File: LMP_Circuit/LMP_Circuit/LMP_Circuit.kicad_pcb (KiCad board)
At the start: 2 copper layers, 126.5 x 91.7 mm, 3 parts

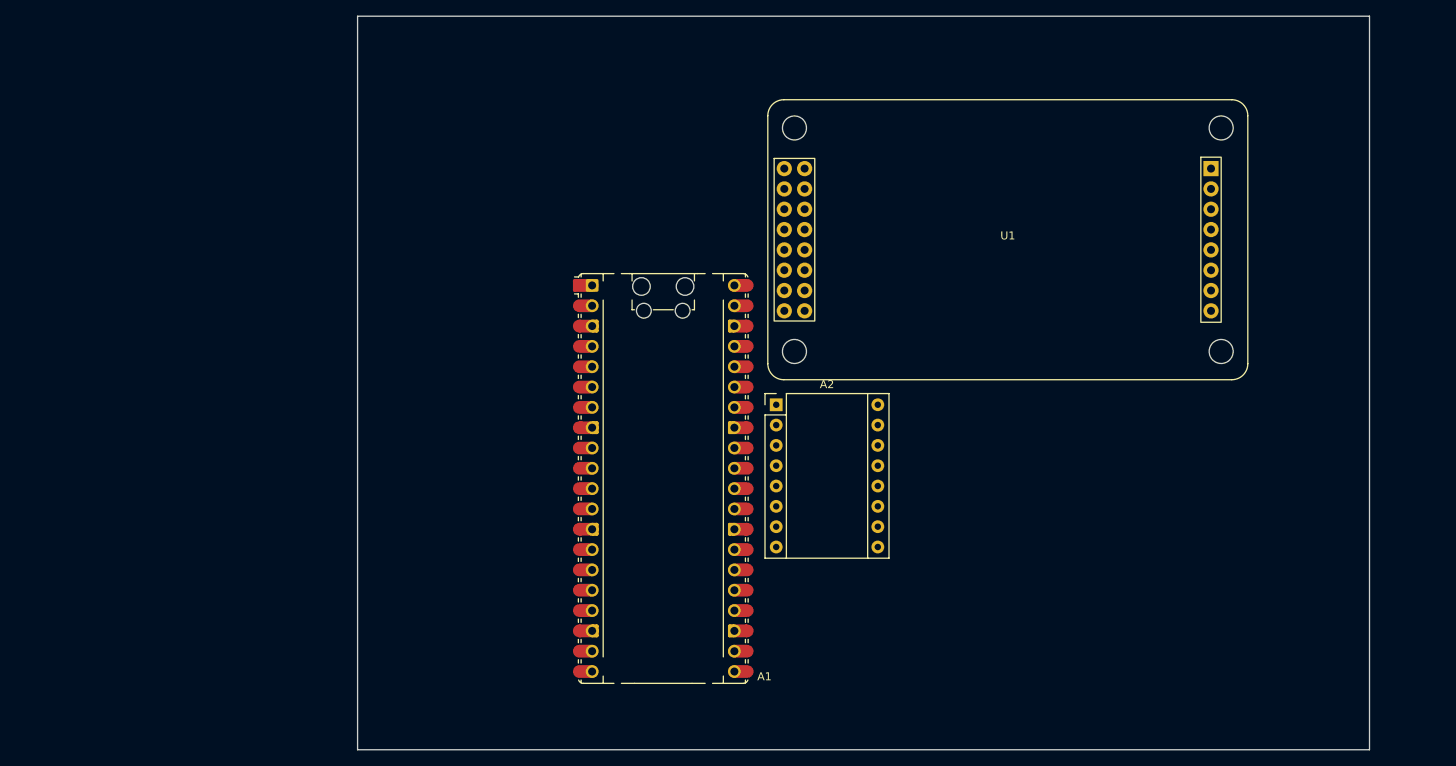
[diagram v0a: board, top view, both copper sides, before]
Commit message: added power converter diagram and relay.
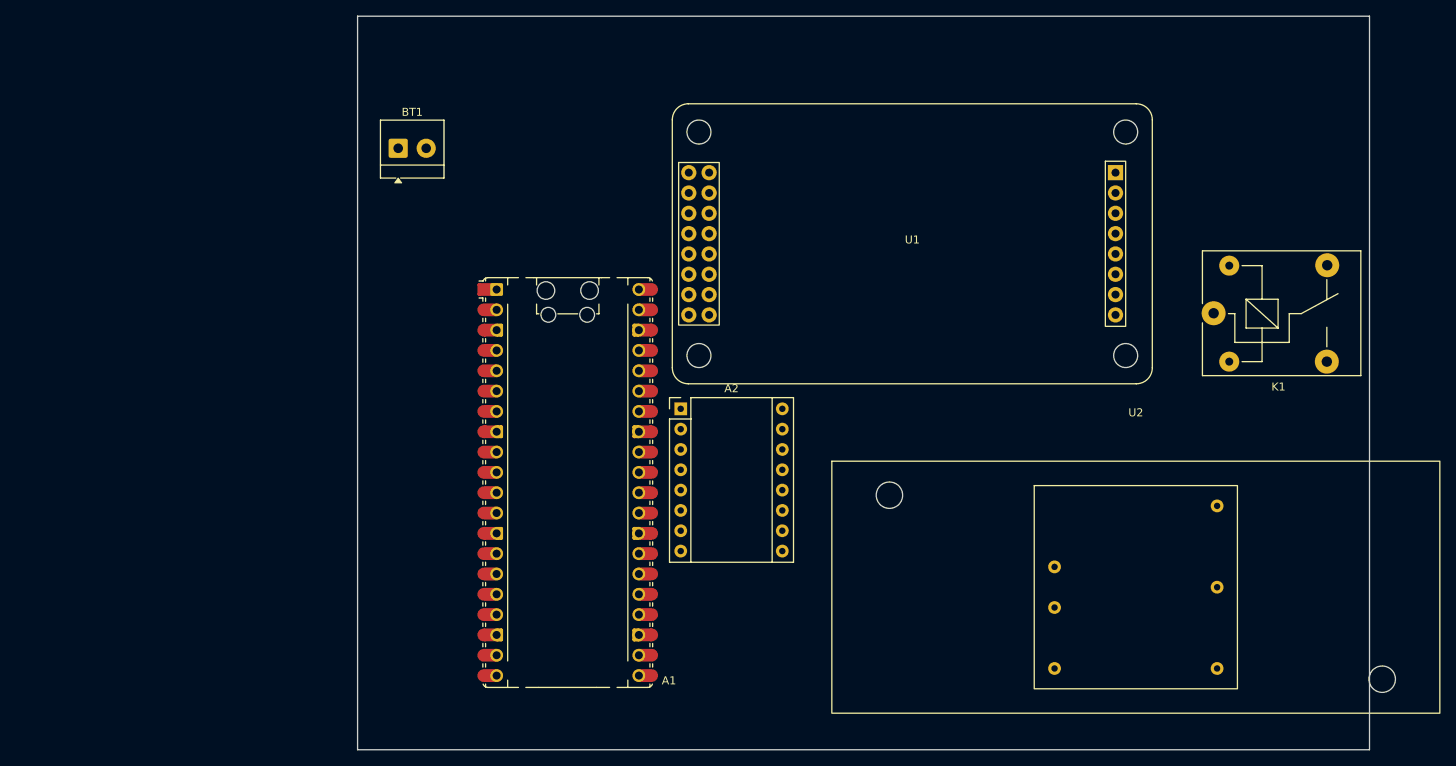
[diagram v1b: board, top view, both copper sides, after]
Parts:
- added BT1: Battery, TerminalBlock_4Ucon:TerminalBlock_4Ucon_1x02_P3.50mm_Horizontal, F.Cu at (104.9, 74.2)
- added K1: SANYOU_SRD_Form_C, Relay_THT:Relay_SPDT_SANYOU_SRD_Series_Form_C, F.Cu at (206.8, 94.8)
- added U2: DQD2_Single, External/Custom Parts:DQD20, F.Cu at (197.1, 129.0)
- moved A1 11.9 mm to (126.1, 116.0)
- moved U1 11.9 mm to (169.2, 86.1)
- moved A2 11.9 mm to (140.2, 106.7)
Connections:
- A1 pad 1: unconnected-(A1-GPIO0-Pad1) -> /Relay_Trigger

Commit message: initial layout created.
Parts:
- removed A2: Pololu_Breakout_A4988, Module:Pololu_Breakout-16_15.2x20.3mm
- removed BT1: Battery, TerminalBlock_4Ucon:TerminalBlock_4Ucon_1x02_P3.50mm_Horizontal
- removed K1: SANYOU_SRD_Form_C, Relay_THT:Relay_SPDT_SANYOU_SRD_Series_Form_C
- removed U2: DQD2_Single, External/Custom Parts:DQD20
- added A3: Pololu_Breakout_A4988, Module:Pololu_Breakout-16_15.2x20.3mm, F.Cu at (125.0, 102.9)
- added C1: 100nf, Capacitor_SMD:C_0603_1608Metric, B.Cu at (110.5, 77.7)
- added C2: 10uf, Capacitor_SMD:C_0603_1608Metric, B.Cu at (114.6, 81.8)
- added C3: 100n, Capacitor_SMD:C_0603_1608Metric, B.Cu at (117.9, 81.8)
- added C4: 10uf, Capacitor_SMD:C_0603_1608Metric, B.Cu at (122.7, 81.8)
- added C5: 100nf, Capacitor_SMD:C_0603_1608Metric, B.Cu at (126.0, 81.8)
- added C6: 10uf, Capacitor_SMD:C_0603_1608Metric, B.Cu at (116.6, 89.4)
- added J1: SCLK, Connector_PinHeader_1.00mm:PinHeader_1x02_P1.00mm_Vertical, B.Cu at (90.5, 112.5)
- added J10: RX, Connector_PinHeader_1.00mm:PinHeader_1x01_P1.00mm_Vertical, B.Cu at (100.1, 133.3)
- added J11: Stepper_Terminals, TerminalBlock_4Ucon:TerminalBlock_4Ucon_1x04_P3.50mm_Horizontal, B.Cu at (122.9, 118.5)
- added J12: ISO_Power_Terminal, TerminalBlock_4Ucon:TerminalBlock_4Ucon_1x02_P3.50mm_Horizontal, B.Cu at (102.9, 76.5)
- added J2: MOSI, Connector_PinHeader_1.00mm:PinHeader_1x02_P1.00mm_Vertical, B.Cu at (87.1, 112.5)
- added J3: MISO, Connector_PinHeader_1.00mm:PinHeader_1x02_P1.00mm_Vertical, B.Cu at (83.8, 112.5)
- added J4: MISO, Connector_PinHeader_1.00mm:PinHeader_1x02_P1.00mm_Vertical, B.Cu at (80.5, 112.5)
- added J5: Relay_Trig, Connector_PinHeader_1.00mm:PinHeader_1x01_P1.00mm_Vertical, B.Cu at (99.8, 122.9)
- added J6: Power Terminal, TerminalBlock_4Ucon:TerminalBlock_4Ucon_1x03_P3.50mm_Horizontal, B.Cu at (117.0, 76.2)
- added J7: Electrode+, Connector_Coaxial:BNC_TEConnectivity_1478035_Horizontal, F.Cu at (74.1, 72.8)
- added J8: Electrode-, Connector_Coaxial:BNC_TEConnectivity_1478035_Horizontal, F.Cu at (91.2, 73.5)
- added J9: TX, Connector_PinHeader_1.00mm:PinHeader_1x01_P1.00mm_Vertical, B.Cu at (100.6, 128.5)
- added R10: 1k, Resistor_SMD:R_0603_1608Metric_Pad0.98x0.95mm_HandSolder, B.Cu at (121.4, 90.9)
- added R11: 1k, Resistor_SMD:R_0603_1608Metric_Pad0.98x0.95mm_HandSolder, B.Cu at (112.8, 103.9)
- added R3: 5M, Resistor_SMD:R_0603_1608Metric_Pad0.98x0.95mm_HandSolder, B.Cu at (116.6, 86.4)
- added R5: 23.57k, Resistor_SMD:R_0603_1608Metric_Pad0.98x0.95mm_HandSolder, B.Cu at (58.4, 110.2)
- added R6: 3.84k, Resistor_SMD:R_0603_1608Metric_Pad0.98x0.95mm_HandSolder, B.Cu at (58.4, 113.8)
- added R7: 23.57k, Resistor_SMD:R_0603_1608Metric_Pad0.98x0.95mm_HandSolder, B.Cu at (58.4, 120.7)
- added R8: 3.84k, Resistor_SMD:R_0603_1608Metric_Pad0.98x0.95mm_HandSolder, B.Cu at (58.4, 124.1)
- added R9: 1M, Resistor_SMD:R_0603_1608Metric_Pad0.98x0.95mm_HandSolder, B.Cu at (121.4, 87.1)
- added U3: ISO124U/1K, External/Custom Parts:ISO124U, B.Cu at (94.9, 93.8)
- added U4: ADS1256, External/Custom Parts:ADS1256, F.Cu at (89.7, 122.9)
- U1: value ~ -> ISO124U/1K; footprint External/Custom Parts:ADS1256 -> External/Custom Parts:ISO124U; moved to B.Cu
- moved U1 93.4 mm to (76.1, 93.8), turned to 90 degrees
- moved A1 47.9 mm to (83.9, 93.2), turned to 90 degrees
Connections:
- A1 pad 1: /Relay_Trigger -> /TX
- A1 pad 2: unconnected-(A1-GPIO1-Pad2) -> /RX
- A1 pad 20: unconnected-(A1-GPIO15-Pad20) -> /PhotoMos
- A1 pad 27: unconnected-(A1-GPIO21-Pad27) -> Net-(A1-GPIO21)
- A1 pad 29: unconnected-(A1-GPIO22-Pad29) -> Net-(A1-GPIO22)
- A1 pad 36: unconnected-(A1-3V3-Pad36) -> +3.3V
- A1 pad 4: unconnected-(A1-GPIO2-Pad4) -> /Relay_Trigger
- U1 pad 1: +5V -> Probe_28V
- U1 pad 13: unconnected-(U1-A4-Pad13) -> Net-(U1-VOUT)
- U1 pad 14: unconnected-(U1-A5-Pad14) -> GND
- U1 pad 15: unconnected-(U1-A6-Pad15) -> 28V
- U1 pad 16: unconnected-(U1-A7-Pad16) -> GND
- U1 pad 2: GND -> GND1
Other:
- board size 126.5 x 91.7 mm -> 70 x 70 mm

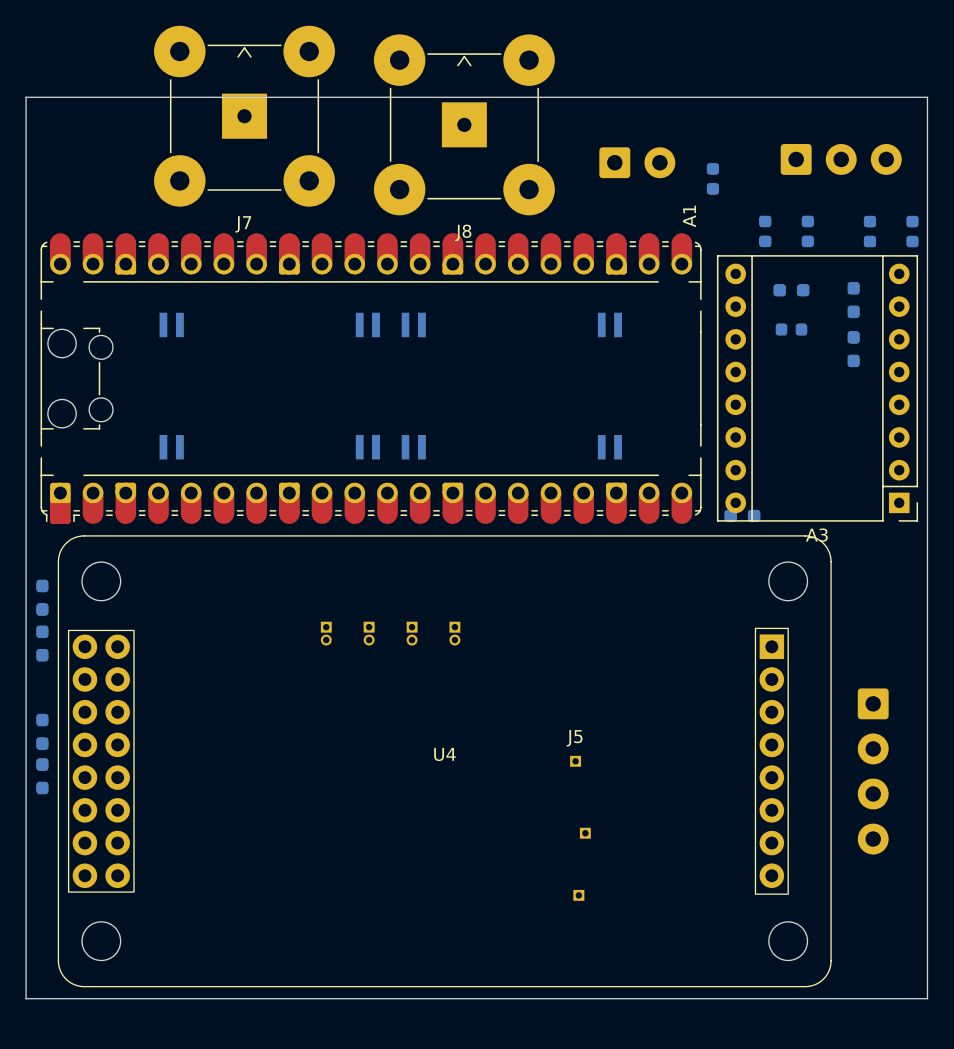
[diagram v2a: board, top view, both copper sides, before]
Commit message: Fully routed, lacks photomosfet
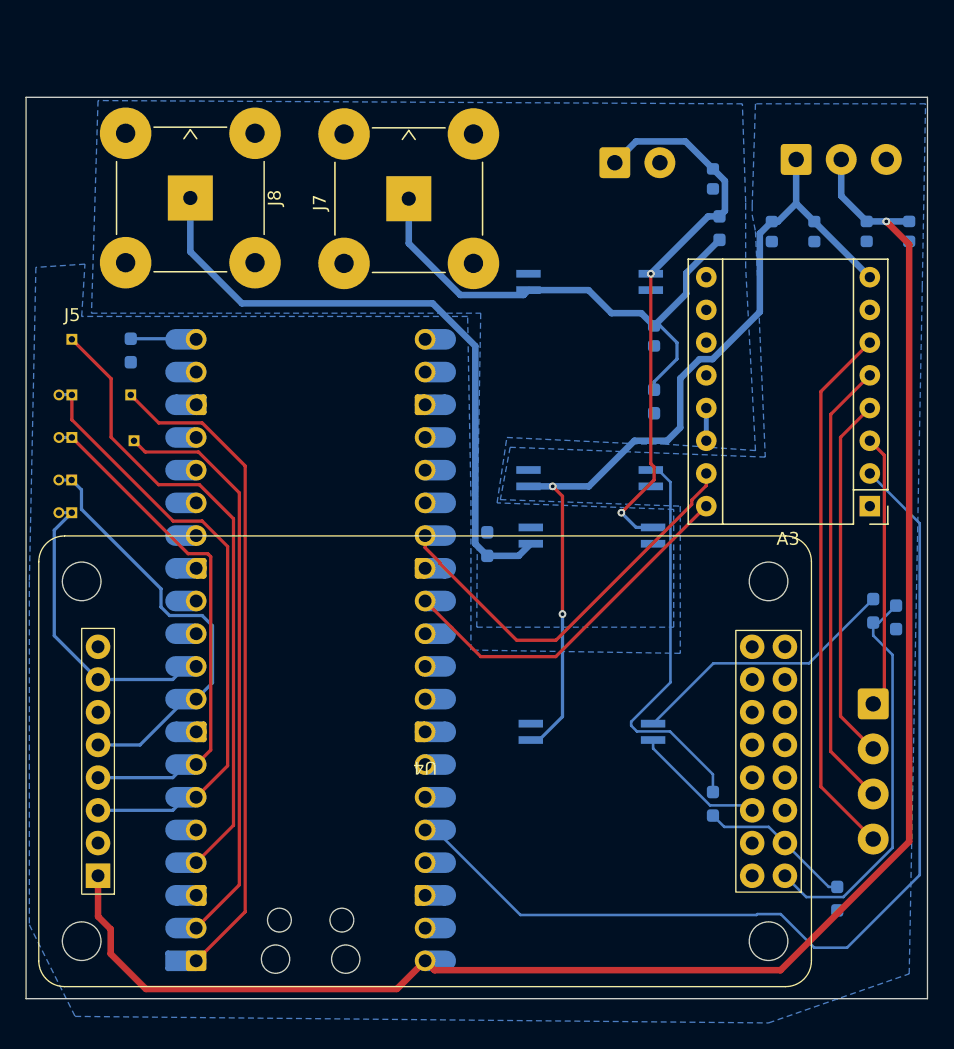
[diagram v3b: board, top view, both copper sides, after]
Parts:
- A1: moved to B.Cu
- moved R6 66.3 mm to (124.7, 111.8)
- moved R5 64.5 mm to (122.9, 111.3)
- moved R8 62.4 mm to (120.1, 133.6)
- moved R7 52.4 mm to (110.5, 126.2)
- moved J5 51.0 mm to (60.7, 90.2)
- moved J10 49.4 mm to (65.5, 98.0), turned to 90 degrees
- moved R11 49.2 mm to (65.3, 91.0), turned to 90 degrees
- moved J9 49.0 mm to (65.3, 94.5), turned to 90 degrees
- moved J1 34.8 mm to (60.7, 94.5), turned to 90 degrees
- moved U1 31.6 mm to (101.1, 113.0), turned to 180 degrees
- moved R3 30.8 mm to (93.0, 106.1), turned to 90 degrees
- moved J2 30.2 mm to (60.7, 97.8), turned to 90 degrees
- moved J3 25.8 mm to (60.7, 101.1), turned to 90 degrees
- moved J8 22.0 mm to (69.9, 79.2)
- moved J4 21.7 mm to (60.7, 103.6), turned to 90 degrees
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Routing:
- net +5V: track 0.00 -> 132.8 mm, vias 0 -> 1
- net +3.3V: track 0.00 -> 76.6 mm
- net 28V: track 0.00 -> 68.6 mm, vias 0 -> 2
- net /TX: track 0.00 -> 51.2 mm
- net /Electrode-: track 0.00 -> 49.8 mm
- net /Relay_Trigger: track 0.00 -> 48.9 mm
- net /SCLK: track 0.00 -> 46.8 mm
- net /RX: track 0.00 -> 45.0 mm
- net Probe_28V: track 0.00 -> 43.3 mm, vias 0 -> 2
- net /2B: track 0.00 -> 41.8 mm
- net /Bias_Sweep: track 0.00 -> 41.0 mm
- net /MOSI: track 0.00 -> 39.5 mm
- net /2A: track 0.00 -> 35.1 mm
- net /MISO: track 0.00 -> 32.9 mm
- net Net-(A1-GPIO21): track 0.00 -> 31.9 mm
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- added copper zone on B.Cu, net GND
- added copper zone on B.Cu, net GND1

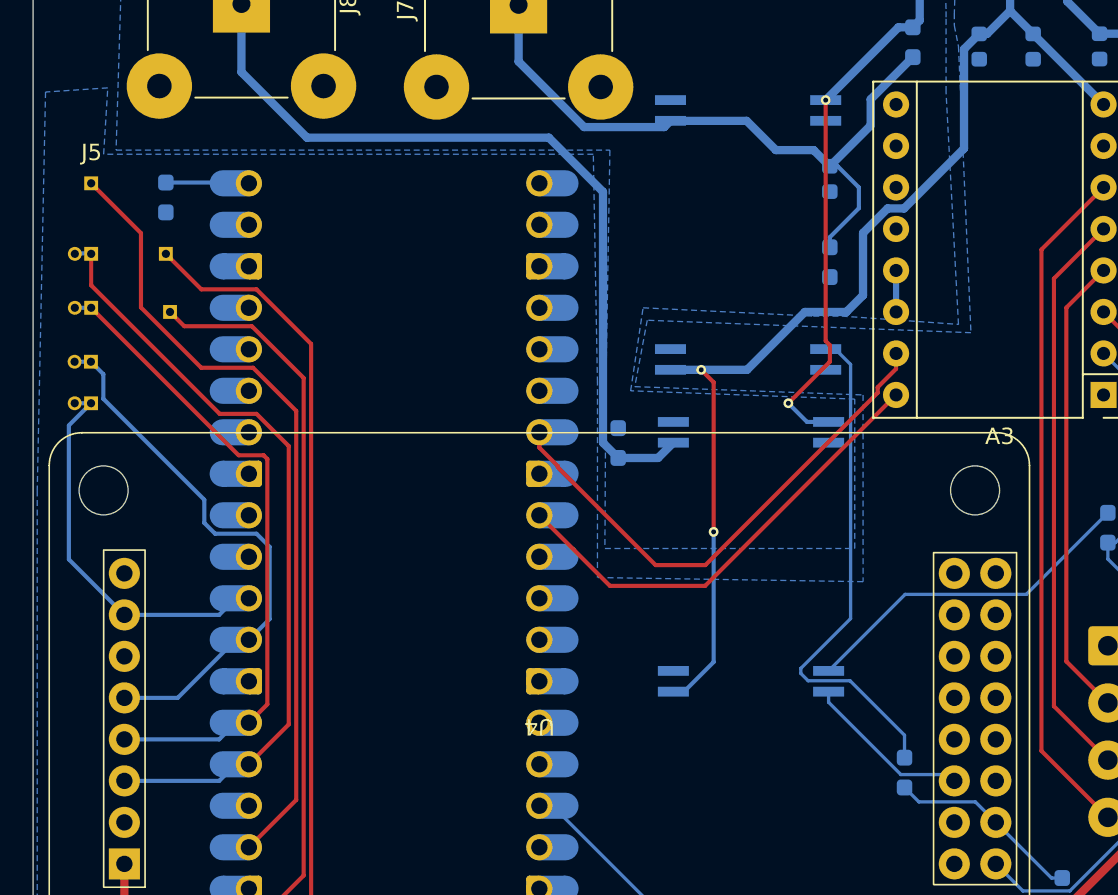
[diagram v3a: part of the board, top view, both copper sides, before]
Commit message: Added Photomos. finished layout
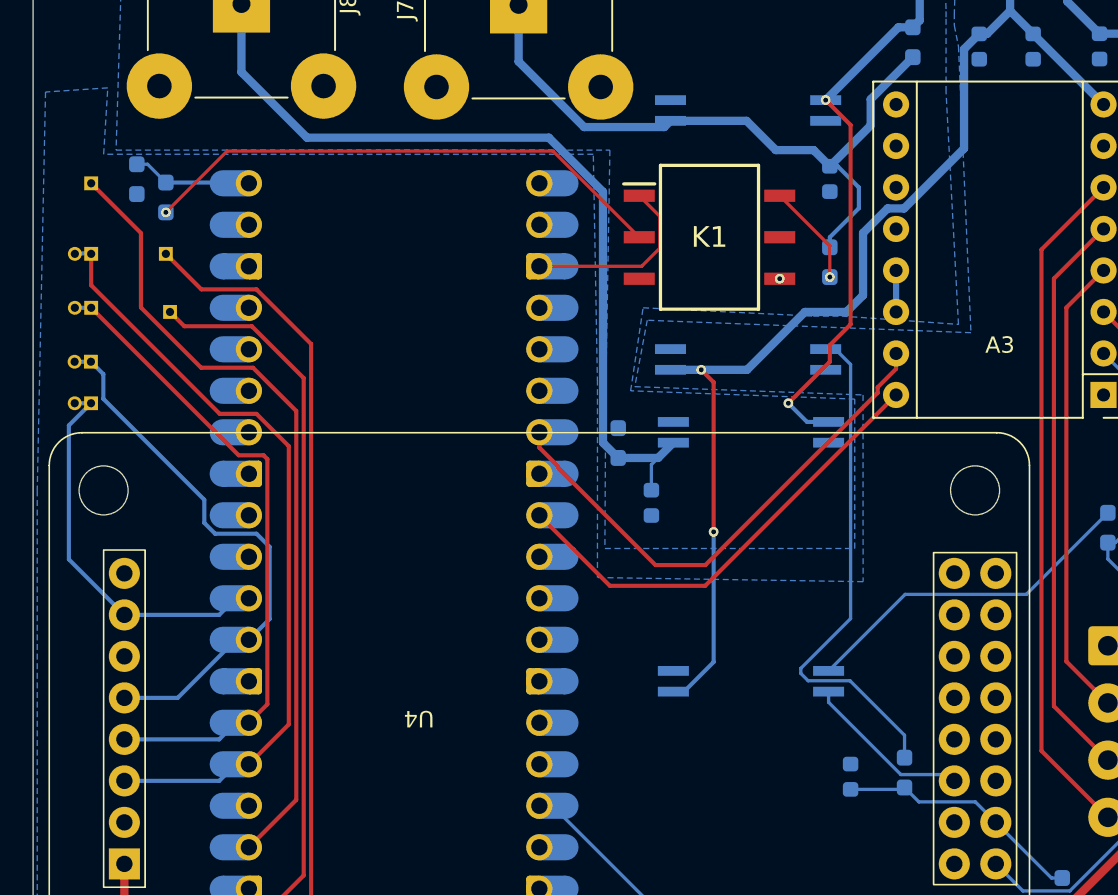
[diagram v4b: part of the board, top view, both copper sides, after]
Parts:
- added C7: 1uf, Capacitor_SMD:C_0603_1608Metric, B.Cu at (107.2, 126.5)
- added C8: 300nf, Capacitor_SMD:C_0603_1608Metric, B.Cu at (95.0, 109.7)
- added K1: AQV101AZ, AQV101AZ:SOP254P960X390-6N, F.Cu at (98.6, 93.5)
- added R1: 1k, Resistor_SMD:R_0603_1608Metric_Pad0.98x0.95mm_HandSolder, B.Cu at (63.5, 89.9)
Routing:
- net Net-(K1-K): track 0.00 -> 32.7 mm, vias 0 -> 1
- net GND: track 10.3 -> 21.9 mm
- net Net-(K1-OUT_2): track 0.00 -> 6.25 mm, vias 0 -> 1
- net /Electrode-: track 49.8 -> 53.2 mm
- net /Bias_Meas: track 11.9 -> 15.3 mm
- net /PhotoMos: track 4.30 -> 6.54 mm
- net Probe_28V: track 43.3 -> 44.3 mm
- net GND1: vias 0 -> 1

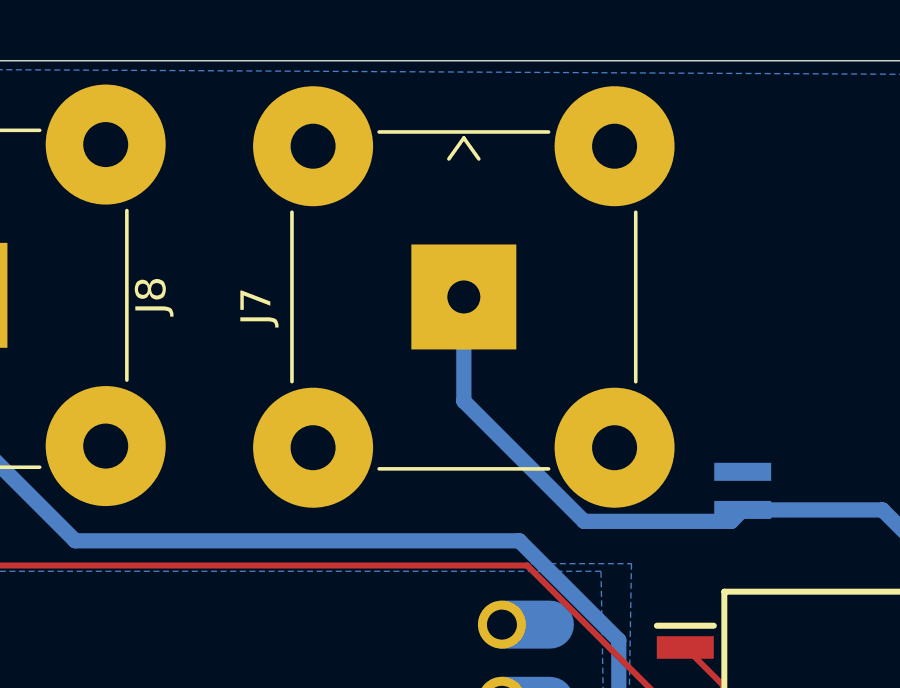
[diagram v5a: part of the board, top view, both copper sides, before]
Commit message: sipm BOM added, files organized a bit more
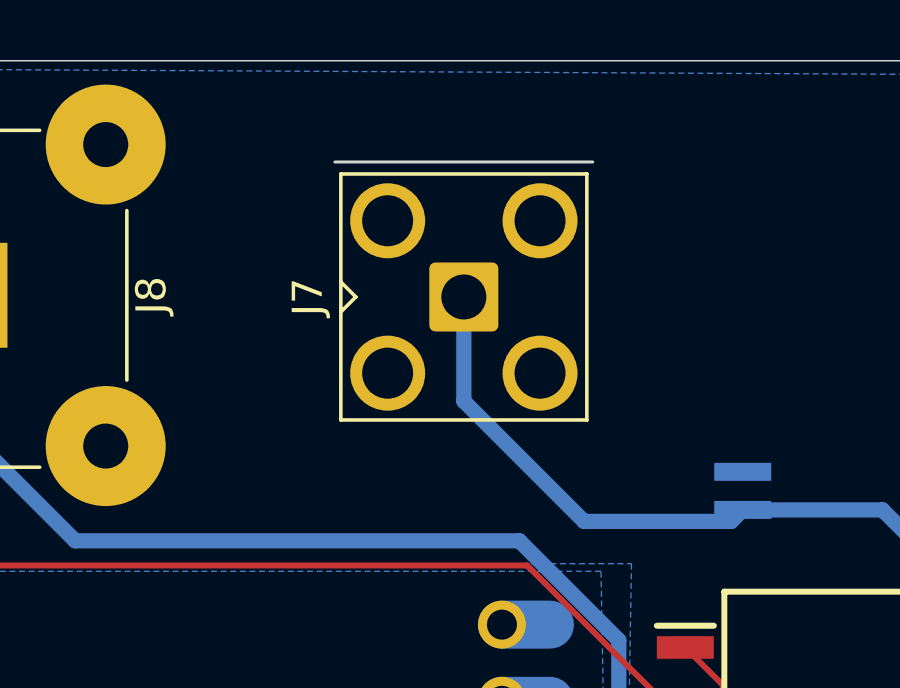
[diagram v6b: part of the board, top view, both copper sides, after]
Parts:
- C3: value 100n -> 100nf
- J7: footprint Connector_Coaxial:BNC_TEConnectivity_1478035_Horizontal -> Connector_Coaxial:SMA_Amphenol_901-143_Horizontal
